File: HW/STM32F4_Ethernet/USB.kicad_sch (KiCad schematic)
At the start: 8 parts

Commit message: Progress backup. add SRAM
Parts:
- gave numbers to parts that had none: 8
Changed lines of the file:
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@@
   (symbol (lib_id "Device:R") (at 176.53 77.47 270) (unit 1)
     (in_bom yes) (on_board yes)
-    (property "Reference" "R?" (id 0) (at 176.53 72.2122 90))
+    (property "Reference" "R33" (id 0) (at 176.53 72.2122 90))
     (property "Value" "22" (id 1) (at 176.53 74.5236 90))
     (property "Footprint" "Resistor_SMD:R_0603_1608Metric_Pad0.98x0.95mm_HandSolder" (id 2) (at 176.53 75.692 90)
@@
   (symbol (lib_id "Device:R") (at 176.53 97.79 270) (unit 1)
     (in_bom yes) (on_board yes)
-    (property "Reference" "R?" (id 0) (at 176.53 100.33 90))
+    (property "Reference" "R34" (id 0) (at 176.53 100.33 90))
     (property "Value" "22" (id 1) (at 176.53 102.87 90))
     (property "Footprint" "Resistor_SMD:R_0603_1608Metric_Pad0.98x0.95mm_HandSolder" (id 2) (at 176.53 96.012 90)
@@
   (symbol (lib_id "power:GNDS") (at 96.52 113.03 0) (unit 1)
     (in_bom yes) (on_board yes) (fields_autoplaced)
-    (property "Reference" "#PWR?" (id 0) (at 96.52 119.38 0)
+    (property "Reference" "#PWR072" (id 0) (at 96.52 119.38 0)
       (effects (font (size 1.27 1.27)) hide)
     )
@@
   (symbol (lib_id "Device:C") (at 100.33 133.35 270) (unit 1)
     (in_bom yes) (on_board yes)
-    (property "Reference" "C?" (id 0) (at 100.33 139.7 90))
+    (property "Reference" "C50" (id 0) (at 100.33 139.7 90))
     (property "Value" "X7R 2nF 2kV " (id 1) (at 100.33 137.16 90))
     (property "Footprint" "" (id 2) (at 96.52 134.3152 0)
@@
   (symbol (lib_id "power:GND") (at 135.89 74.93 90) (unit 1)
     (in_bom yes) (on_board yes)
-    (property "Reference" "#PWR?" (id 0) (at 142.24 74.93 0)
+    (property "Reference" "#PWR076" (id 0) (at 142.24 74.93 0)
       (effects (font (size 1.27 1.27)) hide)
     )
@@
   (symbol (lib_id "power:GND") (at 166.37 87.63 90) (unit 1)
     (in_bom yes) (on_board yes)
-    (property "Reference" "#PWR?" (id 0) (at 172.72 87.63 0)
+    (property "Reference" "#PWR077" (id 0) (at 172.72 87.63 0)
       (effects (font (size 1.27 1.27)) hide)
     )
@@
   (symbol (lib_id "Connector:USB_C_Receptacle_USB2.0") (at 104.14 85.09 0) (unit 1)
     (in_bom yes) (on_board yes) (fields_autoplaced)
-    (property "Reference" "J?" (id 0) (at 104.14 61.595 0))
+    (property "Reference" "J5" (id 0) (at 104.14 61.595 0))
     (property "Value" "USB_C_Receptacle_USB2.0" (id 1) (at 104.14 64.135 0))
     (property "Footprint" "Connector_USB:USB_C_Receptacle_Palconn_UTC16-G" (id 2) (at 107.95 85.09 0)
@@
   (symbol (lib_id "power:GND") (at 104.14 140.97 0) (unit 1)
     (in_bom yes) (on_board yes)
-    (property "Reference" "#PWR?" (id 0) (at 104.14 147.32 0)
+    (property "Reference" "#PWR075" (id 0) (at 104.14 147.32 0)
       (effects (font (size 1.27 1.27)) hide)
     )
@@
   (symbol (lib_id "Power_Protection:USBLC6-2SC6") (at 156.21 87.63 90) (unit 1)
     (in_bom yes) (on_board yes)
-    (property "Reference" "U?" (id 0) (at 161.29 73.66 90)
+    (property "Reference" "U4" (id 0) (at 161.29 73.66 90)
       (effects (font (size 1.27 1.27)) (justify left))
     )
@@
   (symbol (lib_id "power:GND") (at 104.14 113.03 0) (unit 1)
     (in_bom yes) (on_board yes)
-    (property "Reference" "#PWR?" (id 0) (at 104.14 119.38 0)
+    (property "Reference" "#PWR074" (id 0) (at 104.14 119.38 0)
       (effects (font (size 1.27 1.27)) hide)
     )
@@
   (symbol (lib_id "Device:R") (at 100.33 127 270) (unit 1)
     (in_bom yes) (on_board yes)
-    (property "Reference" "R?" (id 0) (at 100.33 129.54 90))
+    (property "Reference" "R30" (id 0) (at 100.33 129.54 90))
     (property "Value" "1M" (id 1) (at 100.33 127 90))
     (property "Footprint" "Resistor_SMD:R_0603_1608Metric_Pad0.98x0.95mm_HandSolder" (id 2) (at 100.33 125.222 90)
@@
   (symbol (lib_id "Device:R_Small") (at 127 74.93 90) (unit 1)
     (in_bom yes) (on_board yes)
-    (property "Reference" "R?" (id 0) (at 127 71.12 90))
+    (property "Reference" "R31" (id 0) (at 127 71.12 90))
     (property "Value" "5.1K" (id 1) (at 127 73.025 90))
     (property "Footprint" "Resistor_SMD:R_0603_1608Metric_Pad0.98x0.95mm_HandSolder" (id 2) (at 127 74.93 0)
@@
   (symbol (lib_id "Device:R_Small") (at 127 77.47 270) (unit 1)
     (in_bom yes) (on_board yes)
-    (property "Reference" "R?" (id 0) (at 127 81.28 90))
+    (property "Reference" "R32" (id 0) (at 127 81.28 90))
     (property "Value" "5.1K" (id 1) (at 127 79.375 90))
     (property "Footprint" "Resistor_SMD:R_0603_1608Metric_Pad0.98x0.95mm_HandSolder" (id 2) (at 127 77.47 0)
@@
   (symbol (lib_id "power:GNDS") (at 96.52 140.97 0) (unit 1)
     (in_bom yes) (on_board yes) (fields_autoplaced)
-    (property "Reference" "#PWR?" (id 0) (at 96.52 147.32 0)
-      (effects (font (size 1.27 1.27)) hide)
-    )
+    (property "Reference" "#PWR073" (id 0) (at 96.52 147.32 0)
+      (effects (font (size 1.27 1.27)) hide)
+    )

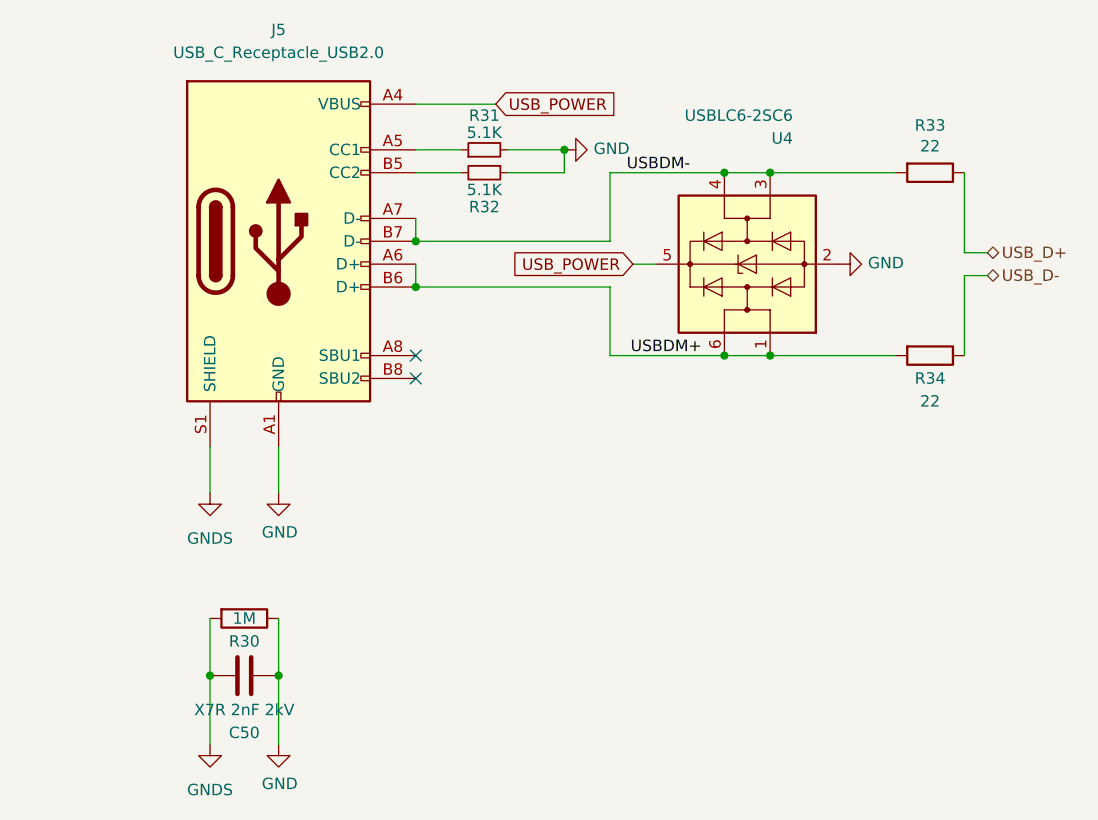
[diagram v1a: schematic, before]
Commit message: Sample PCB. Need to update RLC Size
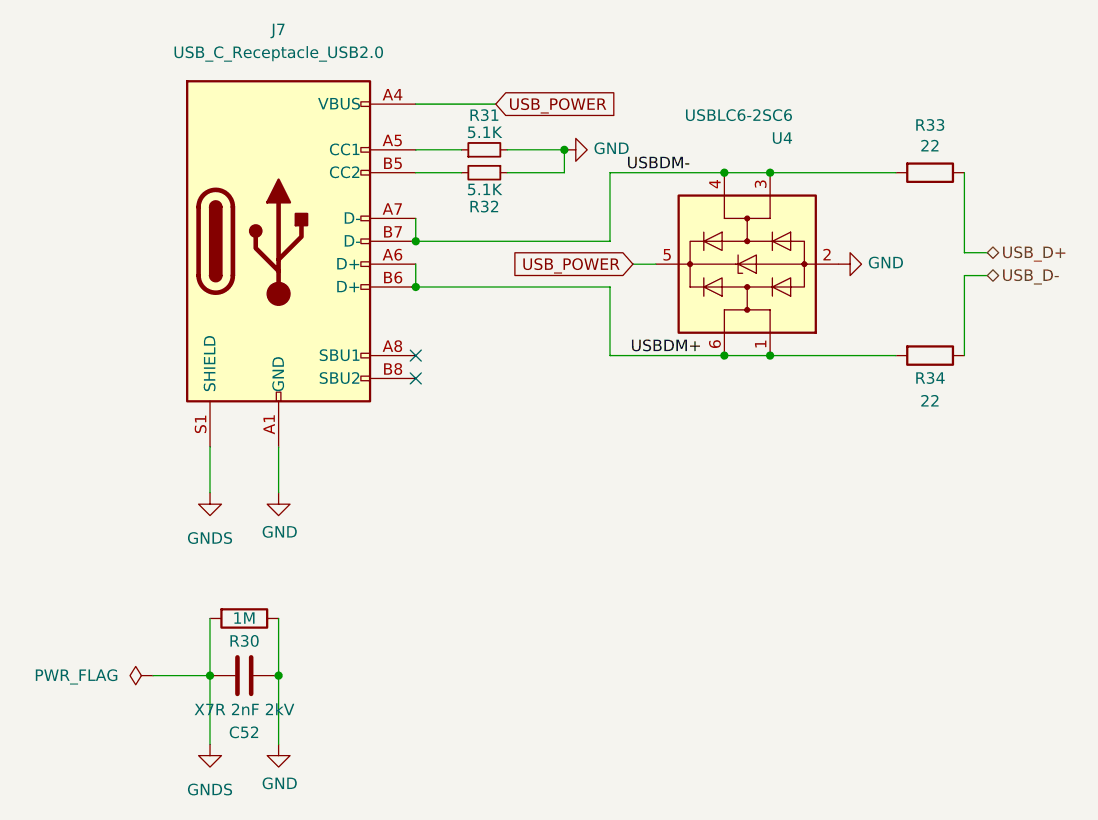
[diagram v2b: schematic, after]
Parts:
- C52: renamed from C50; footprint (none) -> Capacitor_SMD:C_0603_1608Metric_Pad1.08x0.95mm_HandSolder
- renumbered J5 to J7
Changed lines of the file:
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@@
+    (stroke (width 0) (type default) (color 0 0 0 0))
+  )
+  (wire (pts (xy 90.17 133.35) (xy 96.52 133.35))
     (stroke (width 0) (type default) (color 0 0 0 0))
   )
@@
   (symbol (lib_id "power:GNDS") (at 96.52 113.03 0) (unit 1)
     (in_bom yes) (on_board yes) (fields_autoplaced)
-    (property "Reference" "#PWR072" (id 0) (at 96.52 119.38 0)
+    (property "Reference" "#PWR083" (id 0) (at 96.52 119.38 0)
       (effects (font (size 1.27 1.27)) hide)
     )
@@
   (symbol (lib_id "Device:C") (at 100.33 133.35 270) (unit 1)
     (in_bom yes) (on_board yes)
-    (property "Reference" "C50" (id 0) (at 100.33 139.7 90))
+    (property "Reference" "C52" (id 0) (at 100.33 139.7 90))
     (property "Value" "X7R 2nF 2kV " (id 1) (at 100.33 137.16 90))
-    (property "Footprint" "" (id 2) (at 96.52 134.3152 0)
+    (property "Footprint" "Capacitor_SMD:C_0603_1608Metric_Pad1.08x0.95mm_HandSolder" (id 2) (at 96.52 134.3152 0)
       (effects (font (size 1.27 1.27)) hide)
     )
@@
   (symbol (lib_id "power:GND") (at 135.89 74.93 90) (unit 1)
     (in_bom yes) (on_board yes)
-    (property "Reference" "#PWR076" (id 0) (at 142.24 74.93 0)
+    (property "Reference" "#PWR087" (id 0) (at 142.24 74.93 0)
       (effects (font (size 1.27 1.27)) hide)
     )
@@
   (symbol (lib_id "power:GND") (at 166.37 87.63 90) (unit 1)
     (in_bom yes) (on_board yes)
-    (property "Reference" "#PWR077" (id 0) (at 172.72 87.63 0)
+    (property "Reference" "#PWR088" (id 0) (at 172.72 87.63 0)
       (effects (font (size 1.27 1.27)) hide)
     )
@@
   (symbol (lib_id "Connector:USB_C_Receptacle_USB2.0") (at 104.14 85.09 0) (unit 1)
     (in_bom yes) (on_board yes) (fields_autoplaced)
-    (property "Reference" "J5" (id 0) (at 104.14 61.595 0))
+    (property "Reference" "J7" (id 0) (at 104.14 61.595 0))
     (property "Value" "USB_C_Receptacle_USB2.0" (id 1) (at 104.14 64.135 0))
     (property "Footprint" "Connector_USB:USB_C_Receptacle_Palconn_UTC16-G" (id 2) (at 107.95 85.09 0)
@@
   (symbol (lib_id "power:GND") (at 104.14 140.97 0) (unit 1)
     (in_bom yes) (on_board yes)
-    (property "Reference" "#PWR075" (id 0) (at 104.14 147.32 0)
+    (property "Reference" "#PWR086" (id 0) (at 104.14 147.32 0)
       (effects (font (size 1.27 1.27)) hide)
     )
@@
   (symbol (lib_id "power:GND") (at 104.14 113.03 0) (unit 1)
     (in_bom yes) (on_board yes)
-    (property "Reference" "#PWR074" (id 0) (at 104.14 119.38 0)
+    (property "Reference" "#PWR085" (id 0) (at 104.14 119.38 0)
       (effects (font (size 1.27 1.27)) hide)
     )
@@
   (symbol (lib_id "power:GNDS") (at 96.52 140.97 0) (unit 1)
     (in_bom yes) (on_board yes) (fields_autoplaced)
-    (property "Reference" "#PWR073" (id 0) (at 96.52 147.32 0)
+    (property "Reference" "#PWR084" (id 0) (at 96.52 147.32 0)
       (effects (font (size 1.27 1.27)) hide)
     )
@@
       (effects (font (size 1.27 1.27)) hide)
     )
+    (pin "1")
+  )
+  (symbol (lib_id "power:PWR_FLAG") (at 90.17 133.35 90) (unit 1)
+    (in_bom yes) (on_board yes) (fields_autoplaced)
+    (property "Reference" "#FLG09" (id 0) (at 88.265 133.35 0)
+      (effects (font (size 1.27 1.27)) hide)
+    )
+    (property "Value" "PWR_FLAG" (id 1) (at 86.36 133.3499 90)
+      (effects (font (size 1.27 1.27)) (justify left))
+    )
+    (property "Footprint" "" (id 2) (at 90.17 133.35 0)
+      (effects (font (size 1.27 1.27)) hide)
+    )
+    (property "Datasheet" "~" (id 3) (at 90.17 133.35 0)
+      (effects (font (size 1.27 1.27)) hide)
+    )
